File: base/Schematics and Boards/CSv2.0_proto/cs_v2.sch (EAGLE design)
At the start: 80 parts, among them J101 J-JTAG-CORTEX-NEEDLE6-LEGS, J301 HIROSE-DF40_44-PIN_CONNECTORS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, J302 HIROSE-DF40_30-PIN_CONNECTORS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, Q201 FK3303010L, Q202 DMG3415UFY4Q-7, Q203 FK3303010L, Q204 FK3303010L, U101 ATSAMD51, U102 AT25SF641-MHB-T, U201 COULOMB-MAX17262, U202 MAX77827BEWC+T, U203 SENSOR-SI7006, U204 LOADSWITCH-MIC94164, U205 LOADSWITCH-MIC94164, Y101 16M, Y102 ABS07-32.768KHZ-9-T

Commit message: Fix a few items based on 1st round DFM checks with 7pcb
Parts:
- renumbered TP_CPU to CPU, TP_DTR to DTR, TP_PROC to PROC, TP_RX to RXDBG, TP_SCL to SCL, TP_SDA to SDA, TP_STOR to STOR, TP_TEMP to TEMP, TP_TX to TXDBG
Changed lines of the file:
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@@
 <part name="+3V5" library="Supplies" deviceset="+3V3" device=""/>
 <part name="GND18" library="Supplies" deviceset="GND" device=""/>
-<part name="TP_RX" library="TestPoints" deviceset="TP" device="TP06R" package3d_urn="urn:adsk.eagle:package:27954/1" value="TPTP06R"/>
-<part name="TP_TX" library="TestPoints" deviceset="TP" device="TP06R" package3d_urn="urn:adsk.eagle:package:27954/1" value="TPTP06R"/>
+<part name="RXDBG" library="TestPoints" deviceset="TP" device="TP06R" package3d_urn="urn:adsk.eagle:package:27954/1" value="TPTP06R"/>
+<part name="TXDBG" library="TestPoints" deviceset="TP" device="TP06R" package3d_urn="urn:adsk.eagle:package:27954/1" value="TPTP06R"/>
 <part name="R105" library="Resistors" deviceset="R-" device="0402" value="39">
 <attribute name="PART_NO" value="ERJ-2GEJ390X"/>
@@
 <part name="GND14" library="Supplies" deviceset="GND" device=""/>
 <part name="JP203" library="SparkFun-Jumpers" deviceset="JUMPER-SMT_3_1-NC_PASTE" device="_NO-SILK" package3d_urn="urn:adsk.eagle:package:39291/1"/>
-<part name="TP_CPU" library="TestPoints" deviceset="TP" device="TP06R" package3d_urn="urn:adsk.eagle:package:27954/1" value="TPTP06R"/>
-<part name="TP_PROC" library="TestPoints" deviceset="TP" device="TP06R" package3d_urn="urn:adsk.eagle:package:27954/1" value="TPTP06R"/>
-<part name="TP_DTR" library="TestPoints" deviceset="TP" device="TP06R" package3d_urn="urn:adsk.eagle:package:27954/1" value="TPTP06R"/>
-<part name="TP_TEMP" library="TestPoints" deviceset="TP" device="TP06R" package3d_urn="urn:adsk.eagle:package:27954/1" value="TPTP06R"/>
-<part name="TP_STOR" library="TestPoints" deviceset="TP" device="TP06R" package3d_urn="urn:adsk.eagle:package:27954/1" value="TPTP06R"/>
-<part name="TP_SDA" library="TestPoints" deviceset="TP" device="TP06R" package3d_urn="urn:adsk.eagle:package:27954/1" value="TPTP06R"/>
-<part name="TP_SCL" library="TestPoints" deviceset="TP" device="TP06R" package3d_urn="urn:adsk.eagle:package:27954/1" value="TPTP06R"/>
+<part name="CPU" library="TestPoints" deviceset="TP" device="TP06R" package3d_urn="urn:adsk.eagle:package:27954/1" value="TPTP06R"/>
+<part name="PROC" library="TestPoints" deviceset="TP" device="TP06R" package3d_urn="urn:adsk.eagle:package:27954/1" value="TPTP06R"/>
+<part name="DTR" library="TestPoints" deviceset="TP" device="TP06R" package3d_urn="urn:adsk.eagle:package:27954/1" value="TPTP06R"/>
+<part name="TEMP" library="TestPoints" deviceset="TP" device="TP06R" package3d_urn="urn:adsk.eagle:package:27954/1" value="TPTP06R"/>
+<part name="STOR" library="TestPoints" deviceset="TP" device="TP06R" package3d_urn="urn:adsk.eagle:package:27954/1" value="TPTP06R"/>
+<part name="SDA" library="TestPoints" deviceset="TP" device="TP06R" package3d_urn="urn:adsk.eagle:package:27954/1" value="TPTP06R"/>
+<part name="SCL" library="TestPoints" deviceset="TP" device="TP06R" package3d_urn="urn:adsk.eagle:package:27954/1" value="TPTP06R"/>
 <part name="L101" library="Inductors" deviceset="L1212" device="">
 <attribute name="PART_NO" value="LQH3NPN100MMEL"/>
@@
 <attribute name="VALUE" x="307.34" y="213.36" size="1.778" layer="96"/>
 </instance>
-<instance part="TP_RX" gate="G$1" x="33.02" y="152.4" smashed="yes" rot="R90">
+<instance part="RXDBG" gate="G$1" x="33.02" y="152.4" smashed="yes" rot="R90">
 <attribute name="NAME" x="31.75" y="151.384" size="1.778" layer="95" rot="R180"/>
 <attribute name="VALUE" x="31.75" y="154.94" size="1.778" layer="97" rot="R180"/>
 </instance>
-<instance part="TP_TX" gate="G$1" x="50.8" y="152.4" smashed="yes" rot="R90">
+<instance part="TXDBG" gate="G$1" x="50.8" y="152.4" smashed="yes" rot="R90">
 <attribute name="NAME" x="49.53" y="151.384" size="1.778" layer="95" rot="R180"/>
 <attribute name="VALUE" x="49.53" y="154.94" size="1.778" layer="97" rot="R180"/>
@@
 <attribute name="VALUE" x="363.22" y="63.5" size="1.778" layer="96"/>
 </instance>
-<instance part="TP_CPU" gate="G$1" x="231.14" y="187.96" smashed="yes" rot="MR0">
+<instance part="CPU" gate="G$1" x="231.14" y="187.96" smashed="yes" rot="MR0">
 <attribute name="NAME" x="232.156" y="189.23" size="1.778" layer="95" rot="MR90"/>
 </instance>
-<instance part="TP_SDA" gate="G$1" x="259.08" y="200.66" smashed="yes" rot="MR0">
+<instance part="SDA" gate="G$1" x="259.08" y="200.66" smashed="yes" rot="MR0">
 <attribute name="NAME" x="260.096" y="201.93" size="1.778" layer="95" rot="MR90"/>
 </instance>
-<instance part="TP_SCL" gate="G$1" x="223.52" y="200.66" smashed="yes" rot="MR0">
+<instance part="SCL" gate="G$1" x="223.52" y="200.66" smashed="yes" rot="MR0">
 <attribute name="NAME" x="224.536" y="201.93" size="1.778" layer="95" rot="MR90"/>
 </instance>
@@
 <wire x1="231.14" y1="185.42" x2="231.14" y2="182.88" width="0.1524" layer="91"/>
 <junction x="231.14" y="182.88"/>
-<pinref part="TP_CPU" gate="G$1" pin="TP"/>
+<pinref part="CPU" gate="G$1" pin="TP"/>
 <junction x="231.14" y="185.42"/>
 <pinref part="L101" gate="G$1" pin="2"/>
@@
 <wire x1="53.34" y1="149.86" x2="22.86" y2="149.86" width="0.1524" layer="91"/>
 <wire x1="22.86" y1="149.86" x2="20.32" y2="152.4" width="0.1524" layer="91"/>
-<pinref part="TP_TX" gate="G$1" pin="TP"/>
+<pinref part="TXDBG" gate="G$1" pin="TP"/>
 <wire x1="53.34" y1="149.86" x2="53.34" y2="152.4" width="0.1524" layer="91"/>
 <junction x="53.34" y="149.86"/>
@@
 <wire x1="35.56" y1="147.32" x2="22.86" y2="147.32" width="0.1524" layer="91"/>
 <wire x1="22.86" y1="147.32" x2="20.32" y2="149.86" width="0.1524" layer="91"/>
-<pinref part="TP_RX" gate="G$1" pin="TP"/>
+<pinref part="RXDBG" gate="G$1" pin="TP"/>
 <wire x1="35.56" y1="147.32" x2="35.56" y2="152.4" width="0.1524" layer="91"/>
 <junction x="35.56" y="147.32"/>
@@
 <wire x1="254" y1="198.12" x2="259.08" y2="198.12" width="0.1524" layer="91"/>
 <junction x="254" y="198.12"/>
-<pinref part="TP_SDA" gate="G$1" pin="TP"/>
+<pinref part="SDA" gate="G$1" pin="TP"/>
 </segment>
 </net>
@@
 <pinref part="R103" gate="G$1" pin="1"/>
 <label x="228.6" y="203.2" size="1.778" layer="95" rot="R90"/>
-<pinref part="TP_SCL" gate="G$1" pin="TP"/>
+<pinref part="SCL" gate="G$1" pin="TP"/>
 <wire x1="228.6" y1="198.12" x2="223.52" y2="198.12" width="0.1524" layer="91"/>
 <junction x="228.6" y="198.12"/>
@@
 <attribute name="NAME" x="86.36" y="174.879" size="1.778" layer="95" font="vector" rot="R180"/>
 </instance>
-<instance part="TP_PROC" gate="G$1" x="350.52" y="190.5" smashed="yes" rot="MR0">
+<instance part="PROC" gate="G$1" x="350.52" y="190.5" smashed="yes" rot="MR0">
 <attribute name="NAME" x="351.536" y="191.77" size="1.778" layer="95" rot="MR90"/>
 </instance>
-<instance part="TP_DTR" gate="G$1" x="350.52" y="177.8" smashed="yes" rot="MR0">
+<instance part="DTR" gate="G$1" x="350.52" y="177.8" smashed="yes" rot="MR0">
 <attribute name="NAME" x="351.536" y="179.07" size="1.778" layer="95" rot="MR90"/>
 </instance>
-<instance part="TP_TEMP" gate="G$1" x="373.38" y="111.76" smashed="yes" rot="MR0">
+<instance part="TEMP" gate="G$1" x="373.38" y="111.76" smashed="yes" rot="MR0">
 <attribute name="NAME" x="374.396" y="113.03" size="1.778" layer="95" rot="MR90"/>
 </instance>
-<instance part="TP_STOR" gate="G$1" x="373.38" y="152.4" smashed="yes" rot="MR0">
+<instance part="STOR" gate="G$1" x="373.38" y="152.4" smashed="yes" rot="MR0">
 <attribute name="NAME" x="374.396" y="153.67" size="1.778" layer="95" rot="MR90"/>
 </instance>
@@
 <wire x1="373.38" y1="149.86" x2="383.54" y2="149.86" width="0.1524" layer="91"/>
 <wire x1="383.54" y1="149.86" x2="386.08" y2="152.4" width="0.1524" layer="91"/>
-<pinref part="TP_STOR" gate="G$1" pin="TP"/>
+<pinref part="STOR" gate="G$1" pin="TP"/>
 <junction x="373.38" y="149.86"/>
 </segment>
@@
 <wire x1="383.54" y1="175.26" x2="386.08" y2="177.8" width="0.1524" layer="91"/>
 <pinref part="JP205" gate="G$1" pin="1"/>
-<pinref part="TP_DTR" gate="G$1" pin="TP"/>
+<pinref part="DTR" gate="G$1" pin="TP"/>
 <junction x="350.52" y="175.26"/>
 </segment>
@@
 <wire x1="383.54" y1="187.96" x2="386.08" y2="190.5" width="0.1524" layer="91"/>
 <pinref part="JP204" gate="G$1" pin="1"/>
-<pinref part="TP_PROC" gate="G$1" pin="TP"/>
+<pinref part="PROC" gate="G$1" pin="TP"/>
 <junction x="350.52" y="187.96"/>
 </segment>
@@
 <wire x1="373.38" y1="109.22" x2="383.54" y2="109.22" width="0.1524" layer="91"/>
 <wire x1="383.54" y1="109.22" x2="386.08" y2="111.76" width="0.1524" layer="91"/>
-<pinref part="TP_TEMP" gate="G$1" pin="TP"/>
+<pinref part="TEMP" gate="G$1" pin="TP"/>
 <junction x="373.38" y="109.22"/>
 </segment>

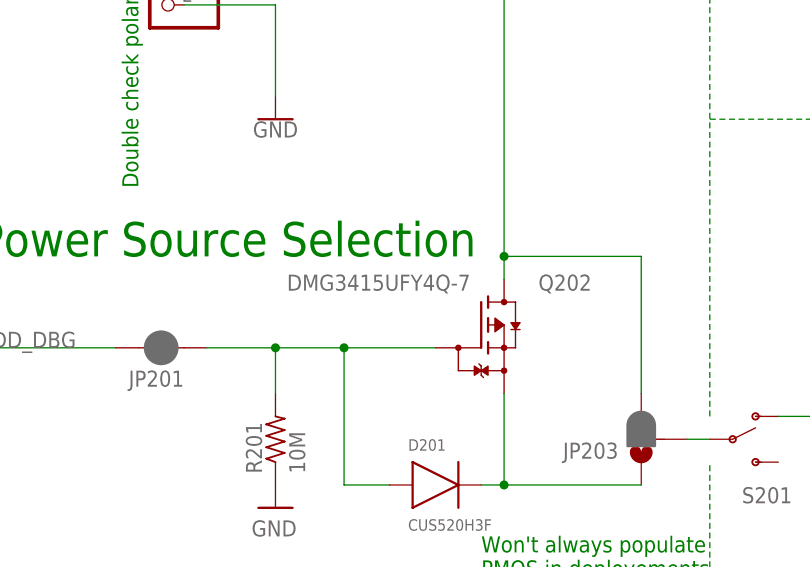
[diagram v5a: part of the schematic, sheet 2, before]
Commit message: Adding item outlines to Eagle as part of DFM issues
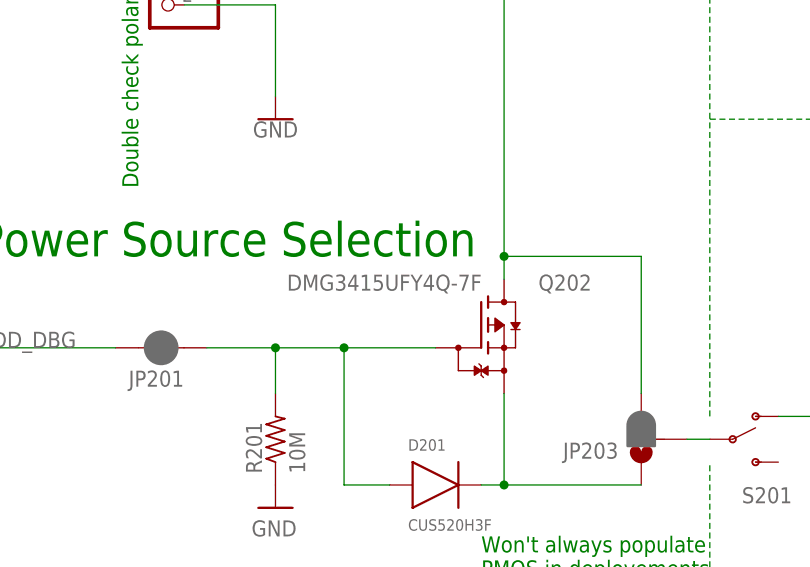
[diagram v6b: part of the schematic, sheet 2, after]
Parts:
- J201: PART_NO SM02B-SRSS-TB(LF)(SN) -> S2B-PH-SM4-TB(LF)(SN)
- Q202: value DMG3415UFY4Q-7 -> DMG3415UFY4Q-7F; device Switches:DMG3415UFY4Q-7 -> Switches:DMG3415UFY4Q-7F
- R103, R104: PART_NO ERJ-3GEYJ472V -> ERJ-2GEJ472X
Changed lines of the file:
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@@
 </part>
 <part name="J201" library="Connectors" deviceset="J-JST2" device="-SMT-RA" package3d_urn="urn:adsk.eagle:package:6240692/1">
-<attribute name="PART_NO" value="SM02B-SRSS-TB(LF)(SN) "/>
+<attribute name="PART_NO" value="S2B-PH-SM4-TB(LF)(SN)"/>
 </part>
 <part name="GND11" library="SparkFun-PowerSymbols" deviceset="GND" device=""/>
@@
 <attribute name="PART_NO" value="DF40HC(3.0)-44DS-0.4V(51)"/>
 </part>
-<part name="Q202" library="Switches" deviceset="DMG3415UFY4Q-7" device="" value="DMG3415UFY4Q-7">
+<part name="Q202" library="Switches" deviceset="DMG3415UFY4Q-7" device="F" value="DMG3415UFY4Q-7F">
 <attribute name="PART_NO" value="DMG3415UFY4Q-7"/>
 </part>
@@
 <part name="+3V6" library="Supplies" deviceset="+3V3" device=""/>
 <part name="R103" library="Resistors" deviceset="R-" device="0402" value="4.7k">
-<attribute name="PART_NO" value="ERJ-3GEYJ472V"/>
+<attribute name="PART_NO" value="ERJ-2GEJ472X"/>
 </part>
 <part name="R104" library="Resistors" deviceset="R-" device="0402" value="4.7k">
-<attribute name="PART_NO" value="ERJ-3GEYJ472V"/>
+<attribute name="PART_NO" value="ERJ-2GEJ472X"/>
 </part>
 <part name="+3V8" library="Supplies" deviceset="+3V3" device=""/>
